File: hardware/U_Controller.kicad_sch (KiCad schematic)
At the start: 11 parts, among them J4 USB_C_Receptacle_USB2.0_14P, SW7 SW_Wuerth_450301014042, U4 STM32C031K6Tx, U5 STM32C071RBT6, Y1 Crystal_GND24

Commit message: chore: update project references
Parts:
- renumbered C67 to C7001, C71 to C7002, D3 to D7001, J4 to J7001, R1 to R7001, R2 to R7002, R3 to R7003, SW7 to SW7001, U4 to U7001, U5 to U7002, Y1 to Y7001
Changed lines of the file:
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@@
 		(dnp no)
 		(fields_autoplaced yes)
-		(property "Reference" "#PWR045"
+		(property "Reference" "#PWR07007"
 			(at 233.68 46.99 0)
 			(effects
@@
 			(project ""
 				(path "/d5303413-7068-41ba-88e3-39dfa38d31b7/027ff087-ab1d-45e5-9d8f-c94102656fe5"
-					(reference "#PWR045")
+					(reference "#PWR07007")
 					(unit 1)
 				)
@@
 		(on_board yes)
 		(dnp no)
-		(property "Reference" "Y1"
+		(property "Reference" "Y7001"
 			(at 31.75 116.84 90)
 			(effects
@@
 			(project ""
 				(path "/d5303413-7068-41ba-88e3-39dfa38d31b7/027ff087-ab1d-45e5-9d8f-c94102656fe5"
-					(reference "Y1")
+					(reference "Y7001")
 					(unit 1)
 				)
@@
 		(on_board yes)
 		(dnp no)
-		(property "Reference" "C67"
+		(property "Reference" "C7001"
 			(at 22.098 110.744 90)
 			(effects
@@
 			(project ""
 				(path "/d5303413-7068-41ba-88e3-39dfa38d31b7/027ff087-ab1d-45e5-9d8f-c94102656fe5"
-					(reference "C67")
+					(reference "C7001")
 					(unit 1)
 				)
@@
 		(on_board yes)
 		(dnp no)
-		(property "Reference" "D3"
+		(property "Reference" "D7001"
 			(at 247.65 35.5599 90)
 			(effects
@@
 			(project ""
 				(path "/d5303413-7068-41ba-88e3-39dfa38d31b7/027ff087-ab1d-45e5-9d8f-c94102656fe5"
-					(reference "D3")
+					(reference "D7001")
 					(unit 1)
 				)
@@
 		(dnp no)
 		(fields_autoplaced yes)
-		(property "Reference" "U4"
+		(property "Reference" "U7001"
 			(at 113.9541 172.72 0)
 			(effects
@@
 			(project ""
 				(path "/d5303413-7068-41ba-88e3-39dfa38d31b7/027ff087-ab1d-45e5-9d8f-c94102656fe5"
-					(reference "U4")
+					(reference "U7001")
 					(unit 1)
 				)
@@
 		(on_board yes)
 		(dnp no)
-		(property "Reference" "#PWR047"
+		(property "Reference" "#PWR07009"
 			(at 267.97 34.29 0)
 			(effects
@@
 			(project ""
 				(path "/d5303413-7068-41ba-88e3-39dfa38d31b7/027ff087-ab1d-45e5-9d8f-c94102656fe5"
-					(reference "#PWR047")
+					(reference "#PWR07009")
 					(unit 1)
 				)
@@
 		(on_board yes)
 		(dnp no)
-		(property "Reference" "C71"
+		(property "Reference" "C7002"
 			(at 22.86 117.348 90)
 			(effects
@@
 			(project "gpu-external-power-supply"
 				(path "/d5303413-7068-41ba-88e3-39dfa38d31b7/027ff087-ab1d-45e5-9d8f-c94102656fe5"
-					(reference "C71")
+					(reference "C7002")
 					(unit 1)
 				)
@@
 		(on_board yes)
 		(dnp no)
-		(property "Reference" "SW7"
+		(property "Reference" "SW7001"
 			(at 256.54 24.13 0)
 			(effects
@@
 			(project ""
 				(path "/d5303413-7068-41ba-88e3-39dfa38d31b7/027ff087-ab1d-45e5-9d8f-c94102656fe5"
-					(reference "SW7")
+					(reference "SW7001")
 					(unit 1)
 				)
@@
 		(dnp no)
 		(fields_autoplaced yes)
-		(property "Reference" "R3"
+		(property "Reference" "R7003"
 			(at 236.22 35.5599 0)
 			(effects
@@
 			(project ""
 				(path "/d5303413-7068-41ba-88e3-39dfa38d31b7/027ff087-ab1d-45e5-9d8f-c94102656fe5"
-					(reference "R3")
+					(reference "R7003")
 					(unit 1)
 				)
@@
 		(dnp no)
 		(fields_autoplaced yes)
-		(property "Reference" "#PWR011"
+		(property "Reference" "#PWR07002"
 			(at 31.75 91.44 0)
 			(effects
@@
 			(project ""
 				(path "/d5303413-7068-41ba-88e3-39dfa38d31b7/027ff087-ab1d-45e5-9d8f-c94102656fe5"
-					(reference "#PWR011")
+					(reference "#PWR07002")
 					(unit 1)
 				)
@@
 		(on_board yes)
 		(dnp no)
-		(property "Reference" "R2"
+		(property "Reference" "R7002"
 			(at 57.15 55.88 90)
 			(effects
@@
 			(project "gpu-external-power-supply"
 				(path "/d5303413-7068-41ba-88e3-39dfa38d31b7/027ff087-ab1d-45e5-9d8f-c94102656fe5"
-					(reference "R2")
+					(reference "R7002")
 					(unit 1)
 				)
@@
 		(dnp no)
 		(fields_autoplaced yes)
-		(property "Reference" "J4"
+		(property "Reference" "J7001"
 			(at 35.56 39.37 0)
 			(effects
@@
 			(project ""
 				(path "/d5303413-7068-41ba-88e3-39dfa38d31b7/027ff087-ab1d-45e5-9d8f-c94102656fe5"
-					(reference "J4")
+					(reference "J7001")
 					(unit 1)
 				)
@@
 		(dnp no)
 		(fields_autoplaced yes)
-		(property "Reference" "#PWR048"
+		(property "Reference" "#PWR07005"
 			(at 113.03 135.89 0)
 			(effects
@@
 			(project ""
 				(path "/d5303413-7068-41ba-88e3-39dfa38d31b7/027ff087-ab1d-45e5-9d8f-c94102656fe5"
-					(reference "#PWR048")
+					(reference "#PWR07005")
 					(unit 1)
 				)
@@
 		(on_board yes)
 		(dnp no)
-		(property "Reference" "R1"
+		(property "Reference" "R7001"
 			(at 57.15 50.8 90)
 			(effects
@@
 			(project ""
 				(path "/d5303413-7068-41ba-88e3-39dfa38d31b7/027ff087-ab1d-45e5-9d8f-c94102656fe5"
-					(reference "R1")
+					(reference "R7001")
 					(unit 1)
 				)
@@
 		(dnp no)
 		(fields_autoplaced yes)
-		(property "Reference" "#PWR032"
+		(property "Reference" "#PWR07001"
 			(at 19.05 129.54 0)
 			(effects
@@
 			(project ""
 				(path "/d5303413-7068-41ba-88e3-39dfa38d31b7/027ff087-ab1d-45e5-9d8f-c94102656fe5"
-					(reference "#PWR032")
+					(reference "#PWR07001")
 					(unit 1)
 				)
@@
 		(dnp no)
 		(fields_autoplaced yes)
-		(property "Reference" "U5"
+		(property "Reference" "U7002"
 			(at 148.59 20.32 0)
 			(effects
@@
 			(project ""
 				(path "/d5303413-7068-41ba-88e3-39dfa38d31b7/027ff087-ab1d-45e5-9d8f-c94102656fe5"
-					(reference "U5")
+					(reference "U7002")
 					(unit 1)
 				)
@@
 		(on_board yes)
 		(dnp no)
-		(property "Reference" "#PWR044"
+		(property "Reference" "#PWR07006"
 			(at 185.42 114.3 0)
 			(effects
@@
 			(project "gpu-external-power-supply"
 				(path "/d5303413-7068-41ba-88e3-39dfa38d31b7/027ff087-ab1d-45e5-9d8f-c94102656fe5"
-					(reference "#PWR044")
+					(reference "#PWR07006")
 					(unit 1)
 				)
@@
 		(on_board yes)
 		(dnp no)
-		(property "Reference" "#PWR013"
+		(property "Reference" "#PWR07004"
 			(at 60.96 63.5 0)
 			(effects
@@
 			(project ""
 				(path "/d5303413-7068-41ba-88e3-39dfa38d31b7/027ff087-ab1d-45e5-9d8f-c94102656fe5"
-					(reference "#PWR013")
+					(reference "#PWR07004")
 					(unit 1)
 				)
@@
 		(dnp no)
 		(fields_autoplaced yes)
-		(property "Reference" "#PWR046"
+		(property "Reference" "#PWR07008"
 			(at 245.11 46.99 0)
 			(effects
@@
 			(project "gpu-external-power-supply"
 				(path "/d5303413-7068-41ba-88e3-39dfa38d31b7/027ff087-ab1d-45e5-9d8f-c94102656fe5"
-					(reference "#PWR046")
+					(reference "#PWR07008")
 					(unit 1)
 				)
@@
 		(dnp no)
 		(fields_autoplaced yes)
-		(property "Reference" "#PWR012"
+		(property "Reference" "#PWR07003"
 			(at 60.96 43.18 0)
 			(effects
@@
 			(project ""
 				(path "/d5303413-7068-41ba-88e3-39dfa38d31b7/027ff087-ab1d-45e5-9d8f-c94102656fe5"
-					(reference "#PWR012")
-					(unit 1)
-				)
+					(reference "#PWR07003")
+					(unit 1)
+				)

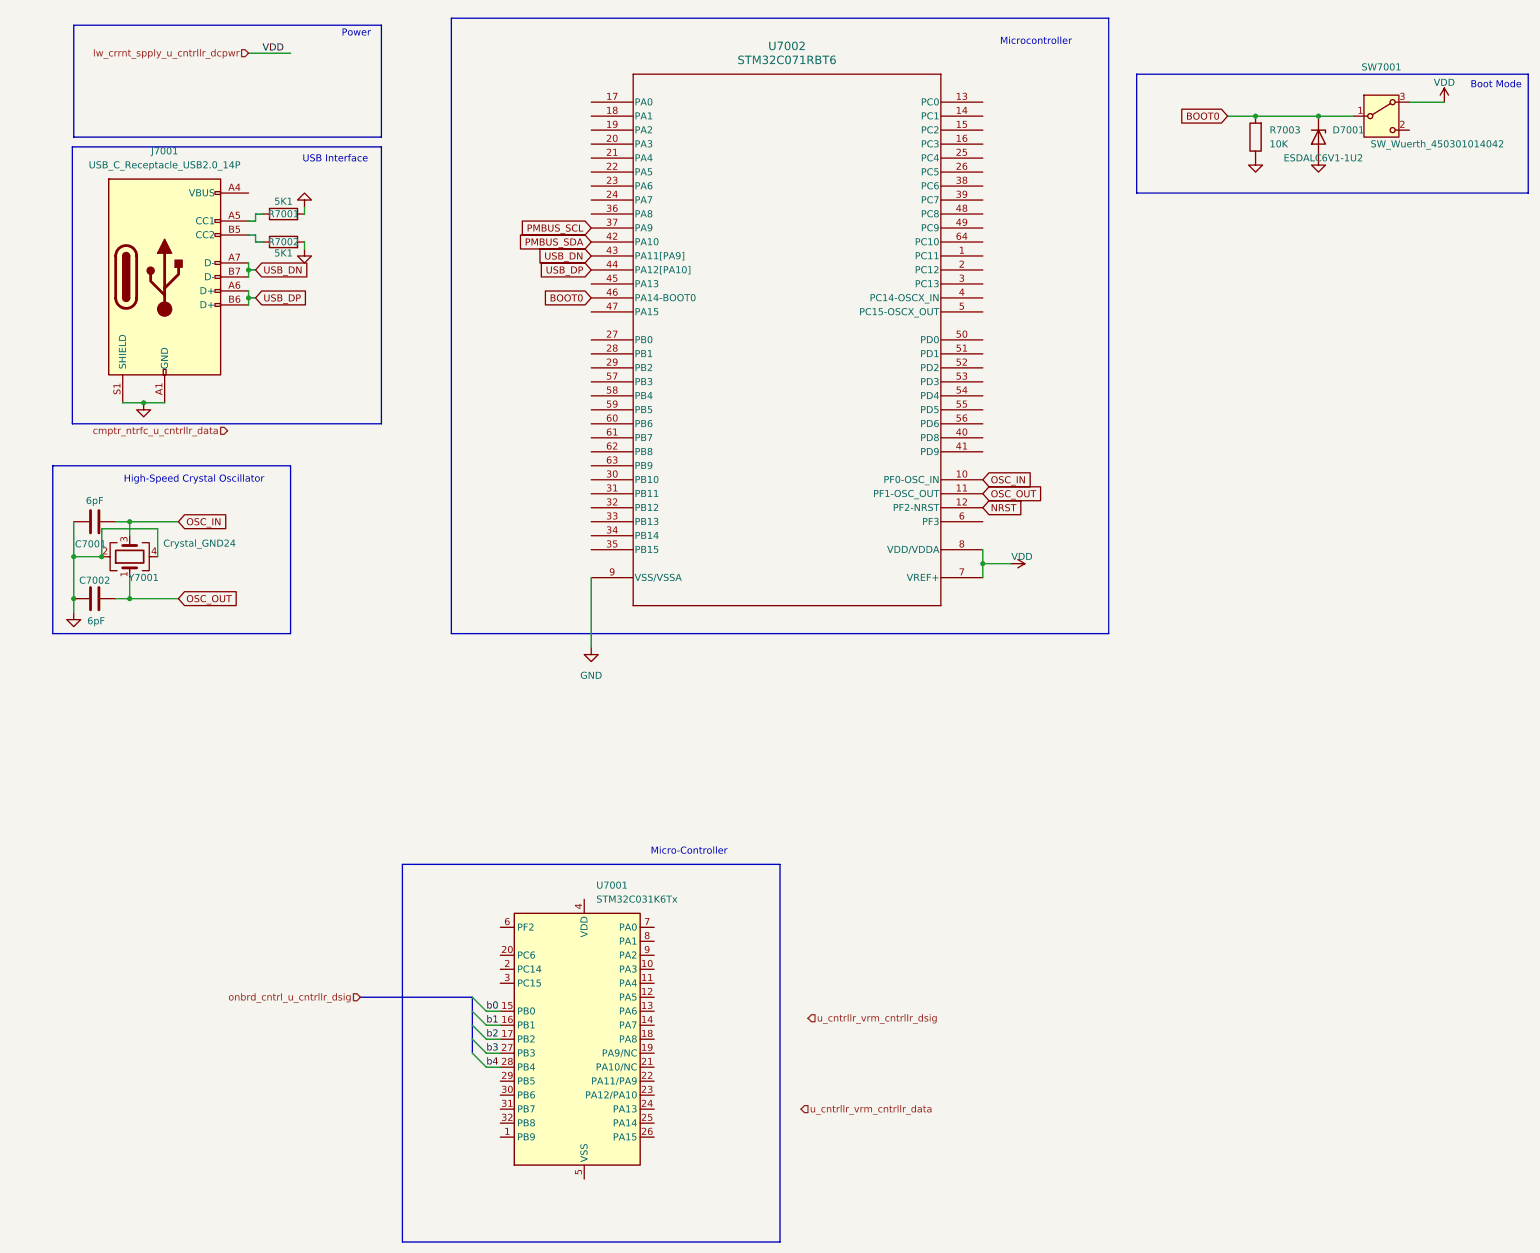
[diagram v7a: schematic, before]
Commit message: feat(schematic): USB-C data line OVP
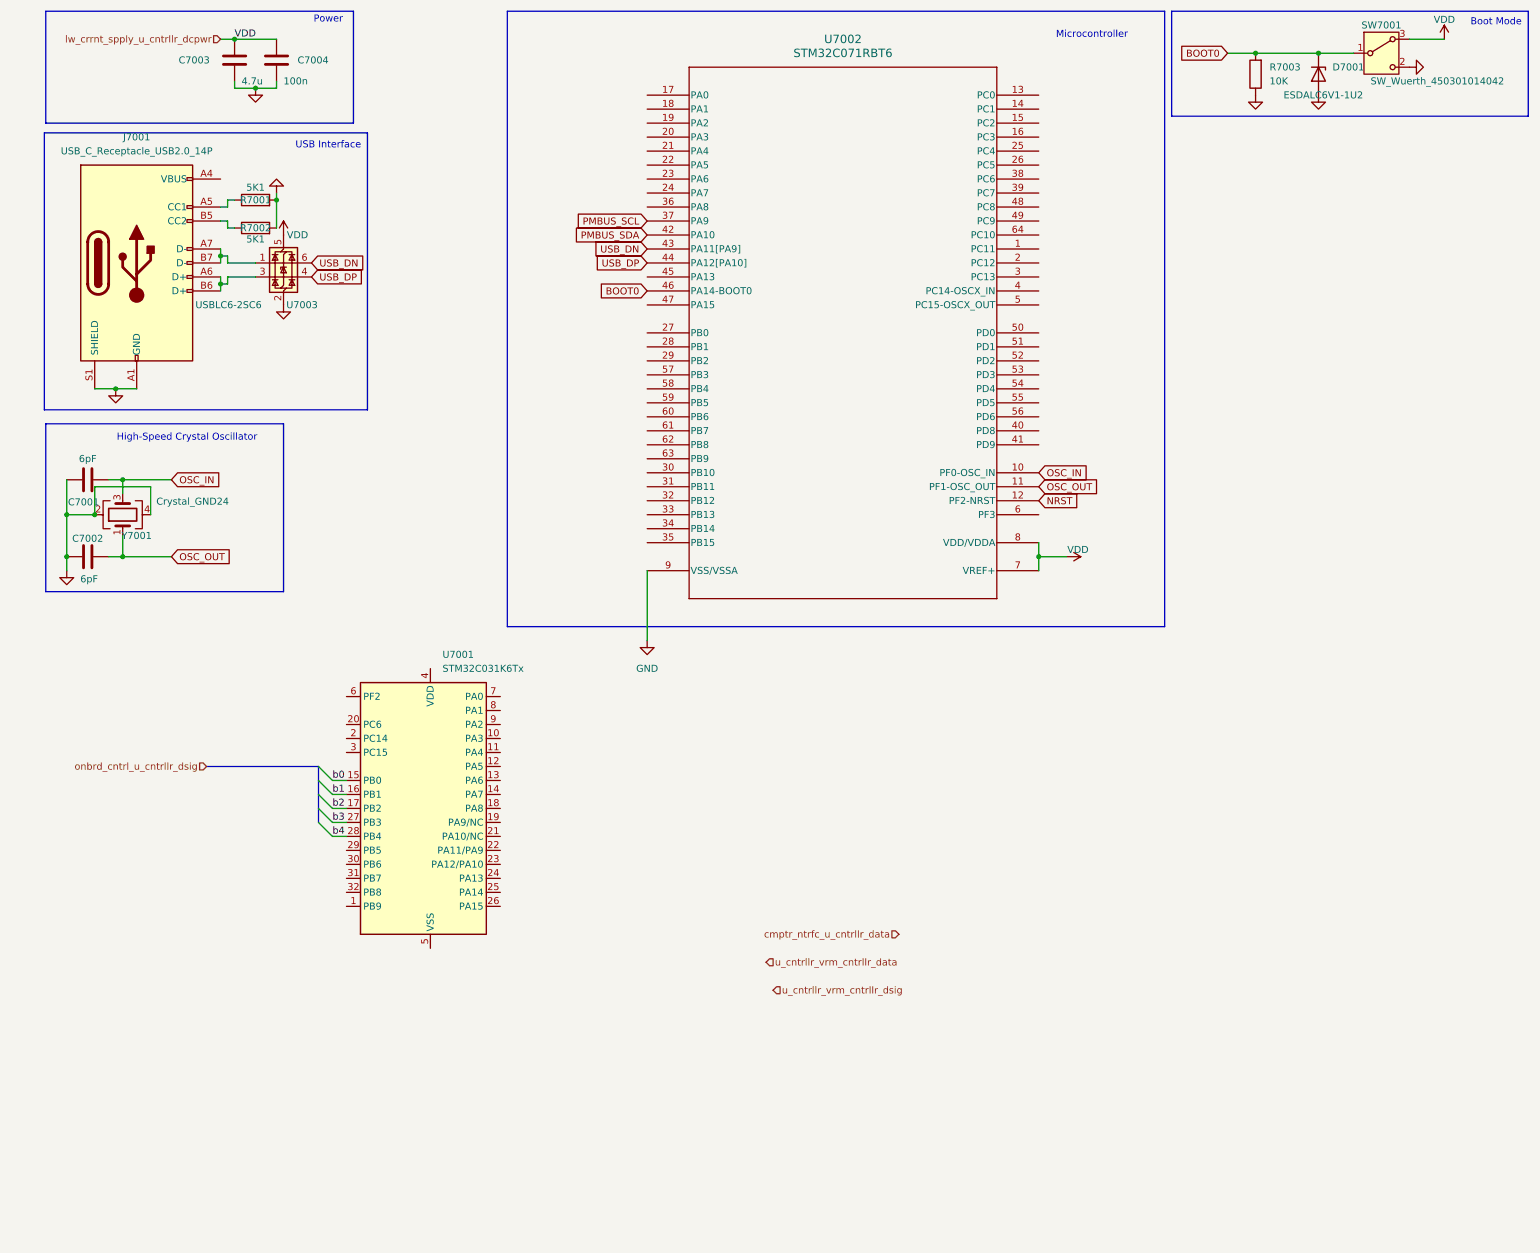
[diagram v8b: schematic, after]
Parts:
- added C7003: 4.7u, symbol Device:C
- added C7004: 100n, symbol Device:C
- added U7003: USBLC6-2SC6, Package_TO_SOT_SMD:SOT-23-6, symbol Power_Protection:USBLC6-2SC6
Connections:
- net GND: now also SW7001.2 (C), C7003.2, C7004.2, U7003.2 (GND)
- net USB_DN: now also U7003.6 (I/O1); no longer J7001.A7 (D-), J7001.B7 (D-)
- net USB_DP: now also U7003.4 (I/O2); no longer J7001.A6 (D+), J7001.B6 (D+)
- net VDD: now also C7003.1, C7004.1, U7003.5 (VBUS)
- new net: J7001.A6 (D+), J7001.B6 (D+), U7003.3 (I/O2)
- new net: J7001.A7 (D-), J7001.B7 (D-), U7003.1 (I/O1)
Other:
- note removed: "Micro-Controller"
- moved on the sheet: C7001, C7002, D7001, J7001, R7001, R7002, R7003, SW7001, U7001, U7002, Y7001
